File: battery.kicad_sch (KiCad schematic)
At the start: 9 parts, among them J1 8-way_Screw, SW3 SW_POWER, U12 ACS758xCB

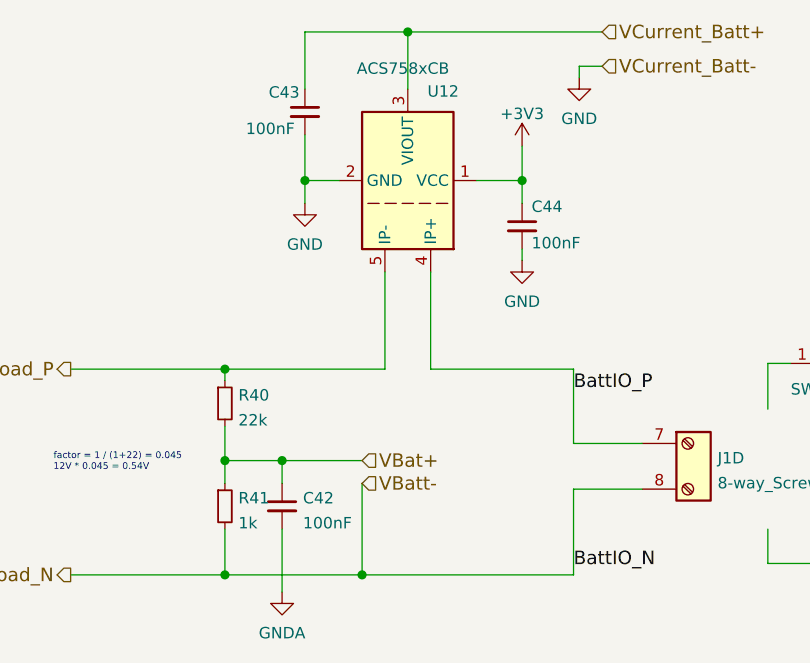
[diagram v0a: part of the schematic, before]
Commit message: Update for Kicad 6-rc; replace 12V reg and cascade; add EEPROM;
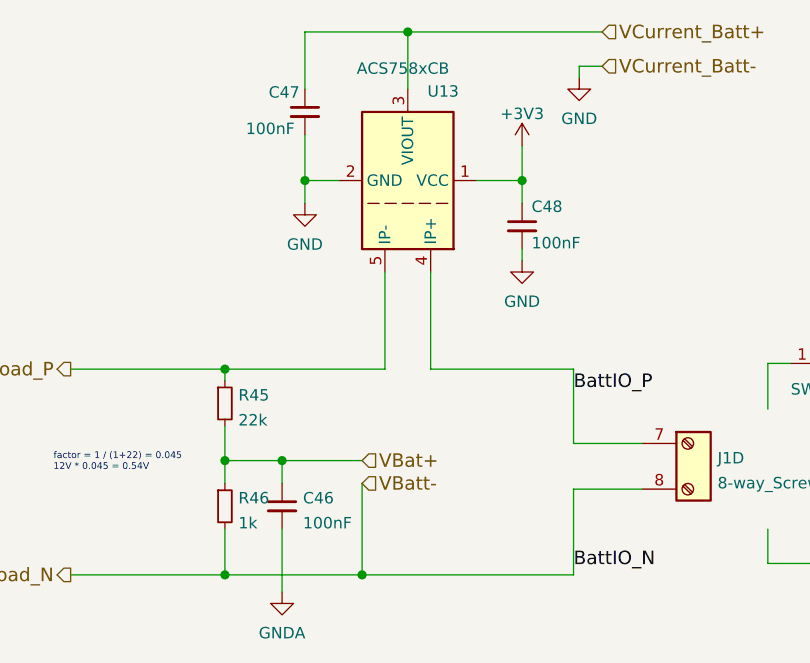
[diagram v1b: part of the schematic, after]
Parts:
- renumbered C42 to C46, C43 to C47, C44 to C48, R40 to R45, R41 to R46, U12 to U13
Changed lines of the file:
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@@
-(kicad_sch (version 20210621) (generator eeschema)
+(kicad_sch (version 20211123) (generator eeschema)
   (paper "A4")
   (title_block
@@
     (company "IvimeyCom")
   )
-  (junction (at 128.905 125.095) (diameter 1.016) (color 0 0 0 0))
-  (junction (at 128.905 102.235) (diameter 1.016) (color 0 0 0 0))
-  (junction (at 149.225 64.77) (diameter 1.016) (color 0 0 0 0))
-  (junction (at 144.145 125.095) (diameter 1.016) (color 0 0 0 0))
-  (junction (at 128.905 112.395) (diameter 1.016) (color 0 0 0 0))
-  (junction (at 137.795 81.28) (diameter 1.016) (color 0 0 0 0))
-  (junction (at 135.255 112.395) (diameter 1.016) (color 0 0 0 0))
-  (junction (at 161.925 81.28) (diameter 1.016) (color 0 0 0 0))
+  (junction (at 137.795 81.28) (diameter 1.016) (color 0 0 0 0)
+  )
+  (junction (at 128.905 125.095) (diameter 1.016) (color 0 0 0 0)
+  )
+  (junction (at 149.225 64.77) (diameter 1.016) (color 0 0 0 0)
+  )
+  (junction (at 135.255 112.395) (diameter 1.016) (color 0 0 0 0)
+  )
+  (junction (at 128.905 112.395) (diameter 1.016) (color 0 0 0 0)
+  )
+  (junction (at 144.145 125.095) (diameter 1.016) (color 0 0 0 0)
+  )
+  (junction (at 161.925 81.28) (diameter 1.016) (color 0 0 0 0)
+  )
+  (junction (at 128.905 102.235) (diameter 1.016) (color 0 0 0 0)
+  )
   (wire (pts (xy 201.93 101.6) (xy 209.55 101.6))
     (stroke (width 0) (type solid) (color 0 0 0 0))
@@
   (symbol (lib_id "power:GND") (at 168.275 69.85 0) (unit 1)
     (in_bom yes) (on_board yes) (fields_autoplaced)
-    (property "Reference" "#PWR075" (id 0) (at 168.275 76.2 0)
+    (property "Reference" "#PWR078" (id 0) (at 168.275 76.2 0)
       (effects (font (size 1.27 1.27)) hide)
     )
@@
   (symbol (lib_id "Device:R_Small") (at 128.905 117.475 0) (unit 1)
     (in_bom yes) (on_board yes)
-    (property "Reference" "R41" (id 0) (at 130.4037 116.5665 0)
+    (property "Reference" "R46" (id 0) (at 130.4037 116.5665 0)
       (effects (font (size 1.27 1.27)) (justify left))
     )
@@
   (symbol (lib_id "power:+3V3") (at 161.925 77.47 0) (unit 1)
     (in_bom yes) (on_board yes) (fields_autoplaced)
-    (property "Reference" "#PWR073" (id 0) (at 161.925 81.28 0)
+    (property "Reference" "#PWR076" (id 0) (at 161.925 81.28 0)
       (effects (font (size 1.27 1.27)) hide)
     )
@@
   (symbol (lib_id "Device:R_Small") (at 128.905 106.045 0) (unit 1)
     (in_bom yes) (on_board yes)
-    (property "Reference" "R40" (id 0) (at 130.4037 105.1365 0)
+    (property "Reference" "R45" (id 0) (at 130.4037 105.1365 0)
       (effects (font (size 1.27 1.27)) (justify left))
     )
@@
   (symbol (lib_id "Device:C_Small") (at 161.925 86.36 0) (unit 1)
     (in_bom yes) (on_board yes)
-    (property "Reference" "C44" (id 0) (at 162.9792 84.1815 0)
+    (property "Reference" "C48" (id 0) (at 162.9792 84.1815 0)
       (effects (font (size 1.27 1.27)) (justify left))
     )
@@
   (symbol (lib_id "power:GND") (at 137.795 83.82 0) (unit 1)
     (in_bom yes) (on_board yes) (fields_autoplaced)
-    (property "Reference" "#PWR072" (id 0) (at 137.795 90.17 0)
+    (property "Reference" "#PWR075" (id 0) (at 137.795 90.17 0)
       (effects (font (size 1.27 1.27)) hide)
     )
@@
   (symbol (lib_id "Sensor_Current:ACS758xCB-050B-PFF") (at 149.225 81.28 270) (mirror x) (unit 1)
     (in_bom yes) (on_board yes)
-    (property "Reference" "U12" (id 0) (at 151.4035 71.3739 90)
+    (property "Reference" "U13" (id 0) (at 151.4035 71.3739 90)
       (effects (font (size 1.27 1.27)) (justify left))
     )
@@
   (symbol (lib_id "Device:C_Small") (at 137.795 73.66 0) (unit 1)
     (in_bom yes) (on_board yes)
-    (property "Reference" "C43" (id 0) (at 133.7692 71.4815 0)
+    (property "Reference" "C47" (id 0) (at 133.7692 71.4815 0)
       (effects (font (size 1.27 1.27)) (justify left))
     )
@@
   (symbol (lib_id "power:GNDA") (at 135.255 127 0) (unit 1)
     (in_bom yes) (on_board yes) (fields_autoplaced)
-    (property "Reference" "#PWR071" (id 0) (at 135.255 133.35 0)
+    (property "Reference" "#PWR074" (id 0) (at 135.255 133.35 0)
       (effects (font (size 1.27 1.27)) hide)
     )
@@
   (symbol (lib_id "Device:C_Small") (at 135.255 117.475 0) (unit 1)
     (in_bom yes) (on_board yes) (fields_autoplaced)
-    (property "Reference" "C42" (id 0) (at 137.5792 116.5665 0)
+    (property "Reference" "C46" (id 0) (at 137.5792 116.5665 0)
       (effects (font (size 1.27 1.27)) (justify left))
     )
@@
   (symbol (lib_id "power:GND") (at 161.925 90.17 0) (unit 1)
     (in_bom yes) (on_board yes) (fields_autoplaced)
-    (property "Reference" "#PWR074" (id 0) (at 161.925 96.52 0)
-      (effects (font (size 1.27 1.27)) hide)
-    )
+    (property "Reference" "#PWR077" (id 0) (at 161.925 96.52 0)
+      (effects (font (size 1.27 1.27)) hide)
+    )

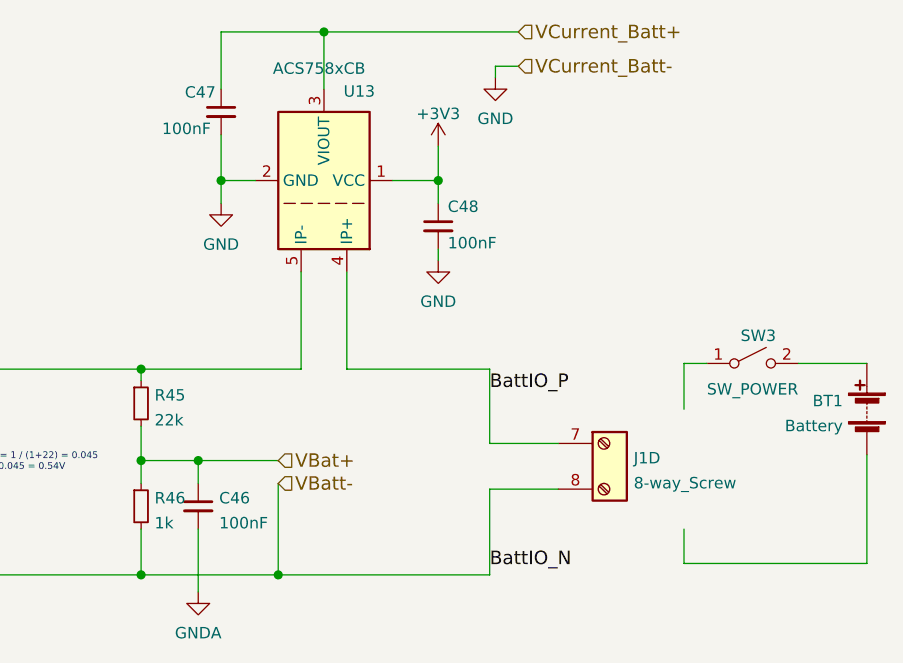
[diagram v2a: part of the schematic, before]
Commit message: Rework with larger display; update component selection; add SWD conn; add RTC chip and QWIIC i2c socket
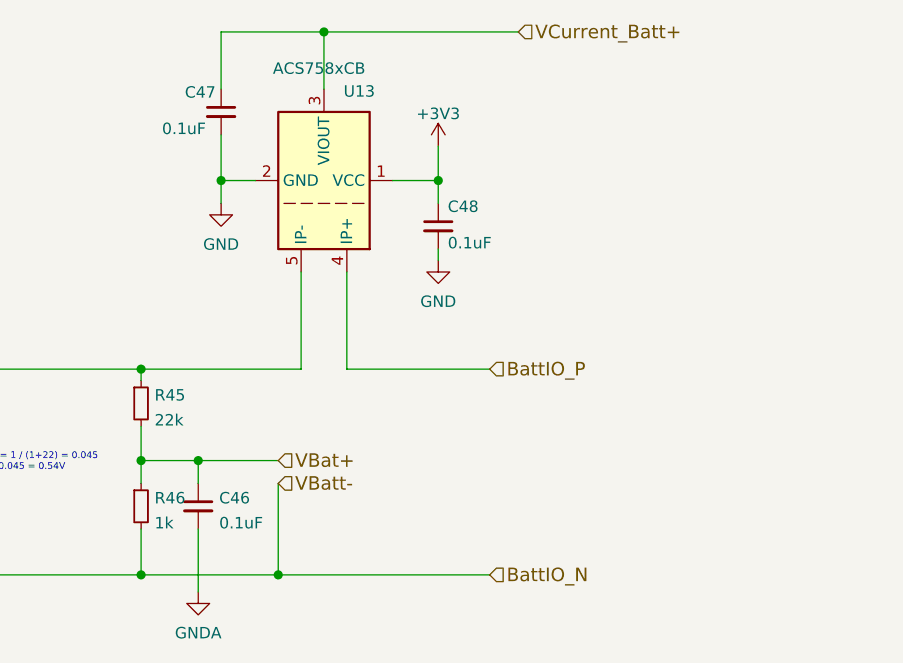
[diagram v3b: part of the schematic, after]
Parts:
- removed BT1: Battery, Connector_Wire:SolderWire-1.5sqmm_1x02_P6mm_D1.7mm_OD3mm, symbol Device:Battery
- removed J1: 8-way_Screw, TerminalBlock_Phoenix:TerminalBlock_Phoenix_MKDS-3-8-5.08_1x08_P5.08mm_Horizontal, symbol solarpump:Screw_Terminal_01x08_4x2U
- removed SW3: SW_POWER, Connector_Wire:SolderWire-0.75sqmm_1x02_P4.8mm_D1.25mm_OD2.3mm, symbol Switch:SW_SPST
- C46, C47, C48: value 100nF -> 0.1uF; Mfr KEMET -> Samsung Electro-Mechanics; Mfr Part No C0402C104K8R7411 -> CL21B104KACNNND; Supl Part No 80-C0402C104K8R7411 -> 187-CL21B104KACNNND
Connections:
- net Load_N renamed BattIO_N

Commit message: More updates to regularise property names
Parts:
- C46, C47, C48: Manuf (none) -> Samsung Electro-Mechanics; Mfr Samsung Electro-Mechanics -> (none); Mfr Part No CL21B104KACNNND -> (none); Part (none) -> CL21B104KACNNND; Supl Mouser -> (none); Supl Part No 187-CL21B104KACNNND -> (none); Supl Price 0.016 -> (none); Vendor (none) -> Mouser; Vendor Cost (none) -> 0.016; Vendor SKU (none) -> 187-CL21B104KACNNND
- R45: Manuf (none) -> Yageo; Mfr Yageo -> (none); Mfr Part No RC0805FR-0722KL -> (none); Part (none) -> RC0805FR-0722KL; Supl Mouser -> (none); Supl Part No 603-RC0805FR-0722KL -> (none); Supl Price 0.077 -> (none); Vendor (none) -> Mouser; Vendor Cost (none) -> 0.077; Vendor SKU (none) -> 603-RC0805FR-0722KL
- R46: Manuf (none) -> Yageo; Mfr Yageo -> (none); Mfr Part No RC0805FR-071KL -> (none); Part (none) -> RC0805FR-071KL; Supl Mouser -> (none); Supl Part No 603-RC0805FR-071KL -> (none); Supl Price 0.077 -> (none); Vendor (none) -> Mouser; Vendor Cost (none) -> 0.077; Vendor SKU (none) -> 603-RC0805FR-071KL
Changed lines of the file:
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@@
       (effects (font (size 1.27 1.27)) hide)
     )
-    (property "Mfr" "Yageo" (id 4) (at 128.905 117.475 0)
-      (effects (font (size 1.27 1.27)) hide)
-    )
-    (property "Mfr Part No" "RC0805FR-071KL" (id 5) (at 128.905 117.475 0)
-      (effects (font (size 1.27 1.27)) hide)
-    )
-    (property "Supl" "Mouser" (id 6) (at 128.905 117.475 0)
-      (effects (font (size 1.27 1.27)) hide)
-    )
-    (property "Supl Part No" "603-RC0805FR-071KL" (id 7) (at 128.905 117.475 0)
-      (effects (font (size 1.27 1.27)) hide)
-    )
-    (property "Supl Price" "0.077" (id 8) (at 128.905 117.475 0)
+    (property "Manuf" "Yageo" (id 4) (at 128.905 117.475 0)
+      (effects (font (size 1.27 1.27)) hide)
+    )
+    (property "Part" "RC0805FR-071KL" (id 5) (at 128.905 117.475 0)
+      (effects (font (size 1.27 1.27)) hide)
+    )
+    (property "Vendor" "Mouser" (id 6) (at 128.905 117.475 0)
+      (effects (font (size 1.27 1.27)) hide)
+    )
+    (property "Vendor SKU" "603-RC0805FR-071KL" (id 7) (at 128.905 117.475 0)
+      (effects (font (size 1.27 1.27)) hide)
+    )
+    (property "Vendor Cost" "0.077" (id 8) (at 128.905 117.475 0)
       (effects (font (size 1.27 1.27)) hide)
     )
@@
       (effects (font (size 1.27 1.27)) hide)
     )
-    (property "Mfr" "Yageo" (id 4) (at 128.905 106.045 0)
-      (effects (font (size 1.27 1.27)) hide)
-    )
-    (property "Mfr Part No" "RC0805FR-0722KL" (id 5) (at 128.905 106.045 0)
-      (effects (font (size 1.27 1.27)) hide)
-    )
-    (property "Supl" "Mouser" (id 6) (at 128.905 106.045 0)
-      (effects (font (size 1.27 1.27)) hide)
-    )
-    (property "Supl Part No" "603-RC0805FR-0722KL" (id 7) (at 128.905 106.045 0)
-      (effects (font (size 1.27 1.27)) hide)
-    )
-    (property "Supl Price" "0.077" (id 8) (at 128.905 106.045 0)
+    (property "Manuf" "Yageo" (id 4) (at 128.905 106.045 0)
+      (effects (font (size 1.27 1.27)) hide)
+    )
+    (property "Part" "RC0805FR-0722KL" (id 5) (at 128.905 106.045 0)
+      (effects (font (size 1.27 1.27)) hide)
+    )
+    (property "Vendor" "Mouser" (id 6) (at 128.905 106.045 0)
+      (effects (font (size 1.27 1.27)) hide)
+    )
+    (property "Vendor SKU" "603-RC0805FR-0722KL" (id 7) (at 128.905 106.045 0)
+      (effects (font (size 1.27 1.27)) hide)
+    )
+    (property "Vendor Cost" "0.077" (id 8) (at 128.905 106.045 0)
       (effects (font (size 1.27 1.27)) hide)
     )
@@
       (effects (font (size 1.27 1.27)) hide)
     )
-    (property "Mfr" "Samsung Electro-Mechanics" (id 4) (at 161.925 86.36 0)
-      (effects (font (size 1.27 1.27)) hide)
-    )
-    (property "Mfr Part No" "CL21B104KACNNND" (id 5) (at 161.925 86.36 0)
-      (effects (font (size 1.27 1.27)) hide)
-    )
-    (property "Supl" "Mouser" (id 6) (at 161.925 86.36 0)
-      (effects (font (size 1.27 1.27)) hide)
-    )
-    (property "Supl Part No" "187-CL21B104KACNNND" (id 7) (at 161.925 86.36 0)
-      (effects (font (size 1.27 1.27)) hide)
-    )
-    (property "Supl Price" "0.016" (id 8) (at 161.925 86.36 0)
+    (property "Manuf" "Samsung Electro-Mechanics" (id 4) (at 161.925 86.36 0)
+      (effects (font (size 1.27 1.27)) hide)
+    )
+    (property "Part" "CL21B104KACNNND" (id 5) (at 161.925 86.36 0)
+      (effects (font (size 1.27 1.27)) hide)
+    )
+    (property "Vendor" "Mouser" (id 6) (at 161.925 86.36 0)
+      (effects (font (size 1.27 1.27)) hide)
+    )
+    (property "Vendor SKU" "187-CL21B104KACNNND" (id 7) (at 161.925 86.36 0)
+      (effects (font (size 1.27 1.27)) hide)
+    )
+    (property "Vendor Cost" "0.016" (id 8) (at 161.925 86.36 0)
       (effects (font (size 1.27 1.27)) hide)
     )
@@
       (effects (font (size 1.27 1.27)) hide)
     )
-    (property "Mfr" "~" (id 4) (at 149.225 81.28 0)
-      (effects (font (size 1.27 1.27)) hide)
-    )
-    (property "Mfr Part No" "~" (id 5) (at 149.225 81.28 0)
-      (effects (font (size 1.27 1.27)) hide)
-    )
-    (property "Supl" "~" (id 6) (at 149.225 81.28 0)
-      (effects (font (size 1.27 1.27)) hide)
-    )
-    (property "Supl Part No" "~" (id 7) (at 149.225 81.28 0)
-      (effects (font (size 1.27 1.27)) hide)
-    )
-    (property "Supl Price" "~" (id 8) (at 149.225 81.28 0)
+    (property "Manuf" "~" (id 4) (at 149.225 81.28 0)
+      (effects (font (size 1.27 1.27)) hide)
+    )
+    (property "Part" "~" (id 5) (at 149.225 81.28 0)
+      (effects (font (size 1.27 1.27)) hide)
+    )
+    (property "Vendor" "~" (id 6) (at 149.225 81.28 0)
+      (effects (font (size 1.27 1.27)) hide)
+    )
+    (property "Vendor SKU" "~" (id 7) (at 149.225 81.28 0)
+      (effects (font (size 1.27 1.27)) hide)
+    )
+    (property "Vendor Cost" "~" (id 8) (at 149.225 81.28 0)
       (effects (font (size 1.27 1.27)) hide)
     )
@@
       (effects (font (size 1.27 1.27)) hide)
     )
-    (property "Mfr" "Samsung Electro-Mechanics" (id 4) (at 137.795 73.66 0)
-      (effects (font (size 1.27 1.27)) hide)
-    )
-    (property "Mfr Part No" "CL21B104KACNNND" (id 5) (at 137.795 73.66 0)
-      (effects (font (size 1.27 1.27)) hide)
-    )
-    (property "Supl" "Mouser" (id 6) (at 137.795 73.66 0)
-      (effects (font (size 1.27 1.27)) hide)
-    )
-    (property "Supl Part No" "187-CL21B104KACNNND" (id 7) (at 137.795 73.66 0)
-      (effects (font (size 1.27 1.27)) hide)
-    )
-    (property "Supl Price" "0.016" (id 8) (at 137.795 73.66 0)
+    (property "Manuf" "Samsung Electro-Mechanics" (id 4) (at 137.795 73.66 0)
+      (effects (font (size 1.27 1.27)) hide)
+    )
+    (property "Part" "CL21B104KACNNND" (id 5) (at 137.795 73.66 0)
+      (effects (font (size 1.27 1.27)) hide)
+    )
+    (property "Vendor" "Mouser" (id 6) (at 137.795 73.66 0)
+      (effects (font (size 1.27 1.27)) hide)
+    )
+    (property "Vendor SKU" "187-CL21B104KACNNND" (id 7) (at 137.795 73.66 0)
+      (effects (font (size 1.27 1.27)) hide)
+    )
+    (property "Vendor Cost" "0.016" (id 8) (at 137.795 73.66 0)
       (effects (font (size 1.27 1.27)) hide)
     )
@@
       (effects (font (size 1.27 1.27)) hide)
     )
-    (property "Mfr" "Samsung Electro-Mechanics" (id 4) (at 135.255 117.475 0)
-      (effects (font (size 1.27 1.27)) hide)
-    )
-    (property "Mfr Part No" "CL21B104KACNNND" (id 5) (at 135.255 117.475 0)
-      (effects (font (size 1.27 1.27)) hide)
-    )
-    (property "Supl" "Mouser" (id 6) (at 135.255 117.475 0)
-      (effects (font (size 1.27 1.27)) hide)
-    )
-    (property "Supl Part No" "187-CL21B104KACNNND" (id 7) (at 135.255 117.475 0)
-      (effects (font (size 1.27 1.27)) hide)
-    )
-    (property "Supl Price" "0.016" (id 8) (at 135.255 117.475 0)
-      (effects (font (size 1.27 1.27)) hide)
-    )
+    (property "Manuf" "Samsung Electro-Mechanics" (id 4) (at 135.255 117.475 0)
+      (effects (font (size 1.27 1.27)) hide)
+    )
+    (property "Part" "CL21B104KACNNND" (id 5) (at 135.255 117.475 0)
+      (effects (font (size 1.27 1.27)) hide)
+    )
+    (property "Vendor" "Mouser" (id 6) (at 135.255 117.475 0)
+      (effects (font (size 1.27 1.27)) hide)
+    )
+    (property "Vendor SKU" "187-CL21B104KACNNND" (id 7) (at 135.255 117.475 0)
+      (effects (font (size 1.27 1.27)) hide)
+    )
+    (property "Vendor Cost" "0.016" (id 8) (at 135.255 117.475 0)
+      (effects (font (size 1.27 1.27)) hide)
+    )

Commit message: Further works...
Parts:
- removed U13: ACS758xCB, solarpump:Allegro_CB_PFF, symbol Sensor_Current:ACS758xCB-050B-PFF
- added C109, C110: 0.1uF,100V, Capacitor_SMD:C_0805_2012Metric_Pad1.18x1.45mm_HandSolder, symbol Device:C_Small
- added D26, D27: B150-E3,50V, Diode_SMD:D_SMA, symbol Device:D_Schottky
- added D28: SMAJ54CA, Diode_SMD:D_SMA, symbol Diode:SMAJ54CA
- added F5: Fuse 25A, Fuse:Fuse_Schurter_UMZ250, symbol Device:Fuse
- added J35: Screw_Terminal_01x02, Connector_Phoenix_MC_HighVoltage:PhoenixContact_MCV_1,5_2-GF-5.08_1x02_P5.08mm_Vertical_ThreadedFlange_MountHole, symbol Connector:Screw_Terminal_01x02
- added Q16: SQM120P10, Package_TO_SOT_SMD:TO-263-2, symbol Transistor_FET:SQM120P10
- added R98: 10k, Resistor_SMD:R_0603_1608Metric, symbol Device:R_Small
- added SW10: SW_SPST, PCM_4ms_Switch:Switch_Toggle_SPST_SubMini, symbol Switch:SW_SPST
- added U31: ACS71240LLCBTR-025B3, Package_SO:SOIC-8_3.9x4.9mm_P1.27mm, symbol Sensor_Current:ACS71240LLCBTR-025B3
- C106: renamed from C47; footprint Capacitor_SMD:C_0805_2012Metric_Pad1.18x1.45mm_HandSolder -> Capacitor_SMD:C_0402_1005Metric
- C107: renamed from C46; footprint Capacitor_SMD:C_0805_2012Metric_Pad1.18x1.45mm_HandSolder -> Capacitor_SMD:C_0402_1005Metric
- C108: renamed from C48; footprint Capacitor_SMD:C_0805_2012Metric_Pad1.18x1.45mm_HandSolder -> Capacitor_SMD:C_0402_1005Metric
- R96: renamed from R45; footprint Resistor_SMD:R_0805_2012Metric_Pad1.20x1.40mm_HandSolder -> Resistor_SMD:R_0603_1608Metric
- R97: renamed from R46; footprint Resistor_SMD:R_0805_2012Metric_Pad1.20x1.40mm_HandSolder -> Resistor_SMD:R_0603_1608Metric
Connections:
- net GNDA is gone; now on net GND: C107.2
- net +3V3: now also U31.8 (VCC)
- net BattIO_P: now also C110.2, D28.2 (A2), F5.2, Q16.2 (D)
- net GND: now also D26.2 (A), U31.5 (GND)
- net Load_P: now also U31.3 (IP-), U31.4 (IP-)
- net BattIO_N renamed Load_N
- net Load_N: now also D28.1 (A1), J35.2 (Pin_2), R98.2
- net VCurrent_Batt+ renamed VCur_Batt+
- net VCur_Batt+: now also U31.7 (VIOUT)
- new net: C109.1, C110.1, D27.2 (A), Q16.1 (G), R98.1
- new net: J35.1 (Pin_1), SW10.2 (B)
- new net: F5.1, SW10.1 (A)
- new net +BattPwr: C109.2, D26.1 (K), D27.1 (K), Q16.3 (S), U31.1 (IP+), U31.2 (IP+)
- new net BattCurSns_Fault: U31.6 (~{FAULT})
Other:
- title: SolarPump v3 -> SolarPump v4
- moved on the sheet: C106, C107, C108, R96, R97
